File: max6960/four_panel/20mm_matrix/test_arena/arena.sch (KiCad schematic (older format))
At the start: 29 parts, among them P1 CONN15, P10 CONN_2X2, P11 CONN_2X2, P12 CONN_2X2, P13 CONN_2X2, P14 CONN_2X2, P15 CONN_2X2, P16 CONN_2X2, P17 CONN_2X2, P18 CONN_2X2, P19 CONN_2X2, P2 CONN15, P20 CONN_2X2, P21 CONN_2X2, P22 CONN_20X2, P23 CONN_30X2, P24 CONN_2, P3 CONN15, P4 CONN15, P5 CONN15, P6 CONN15, P7 CONN_2X2, P8 CONN_2X2, P9 CONN_2X2

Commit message: Finished 4x20mm matrix MAX6960 test arena.
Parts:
- added C6: 0.1uF, symbol C
- added P25: CONN_2X2, symbol CONN_2X2
- added P26: CONN_2, symbol CONN_2
- added U1: MAX7375, symbol MAX7375
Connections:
- net labels added: +3.3V, CLK_0, CLK_1, CLK_11, CLK_2, CLK_22, CLK_3, CLK_33, CLK_4, CLK_44, CLK_5, CLK_55, INT_OSC, OSC, OSC_EXT, OSC_INT, RST, VAUX
- net labels removed: +5V, EXT_INT0, EXT_INT1, RESET_MSTR, RX, SCK_0, SCK_1, SCK_11, SCK_2, SCK_22, SCK_3, SCK_33, SCK_4, SCK_44, SCK_5, SCK_55, TX
- wire segments 300 -> 299
- no-connect marks 3 -> 21
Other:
- note added: "Internal Oscillator"
- note added: "MAX7375AXR805+ (8MHz)"
- note added: "Oscillator Selection"
- moved on the sheet: C1, C2, C3, C4, C5, P22, P23, P24

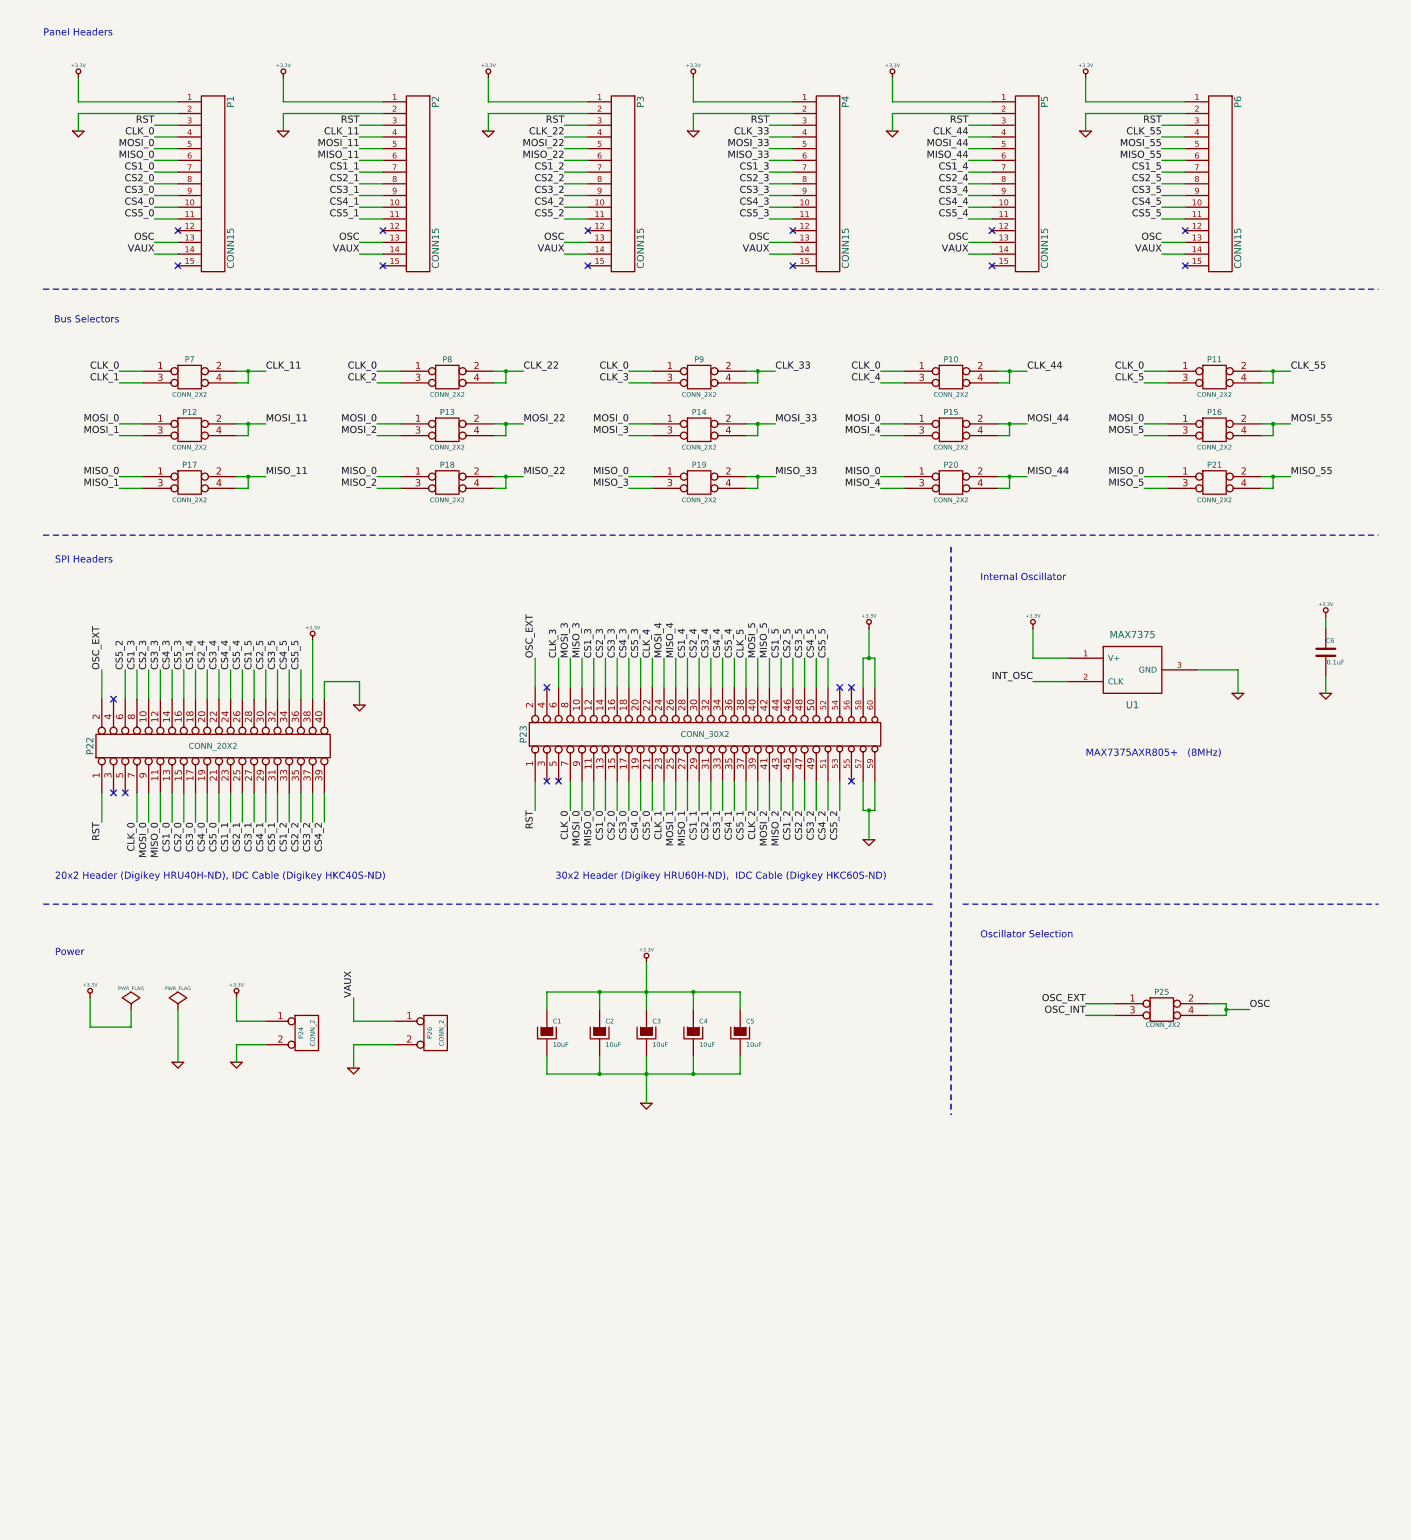
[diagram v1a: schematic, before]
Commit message: Added common CS SPI header to 4x20mm max6960 test arena. Fixed minor issue with 4x20mm atmega328 test arena.
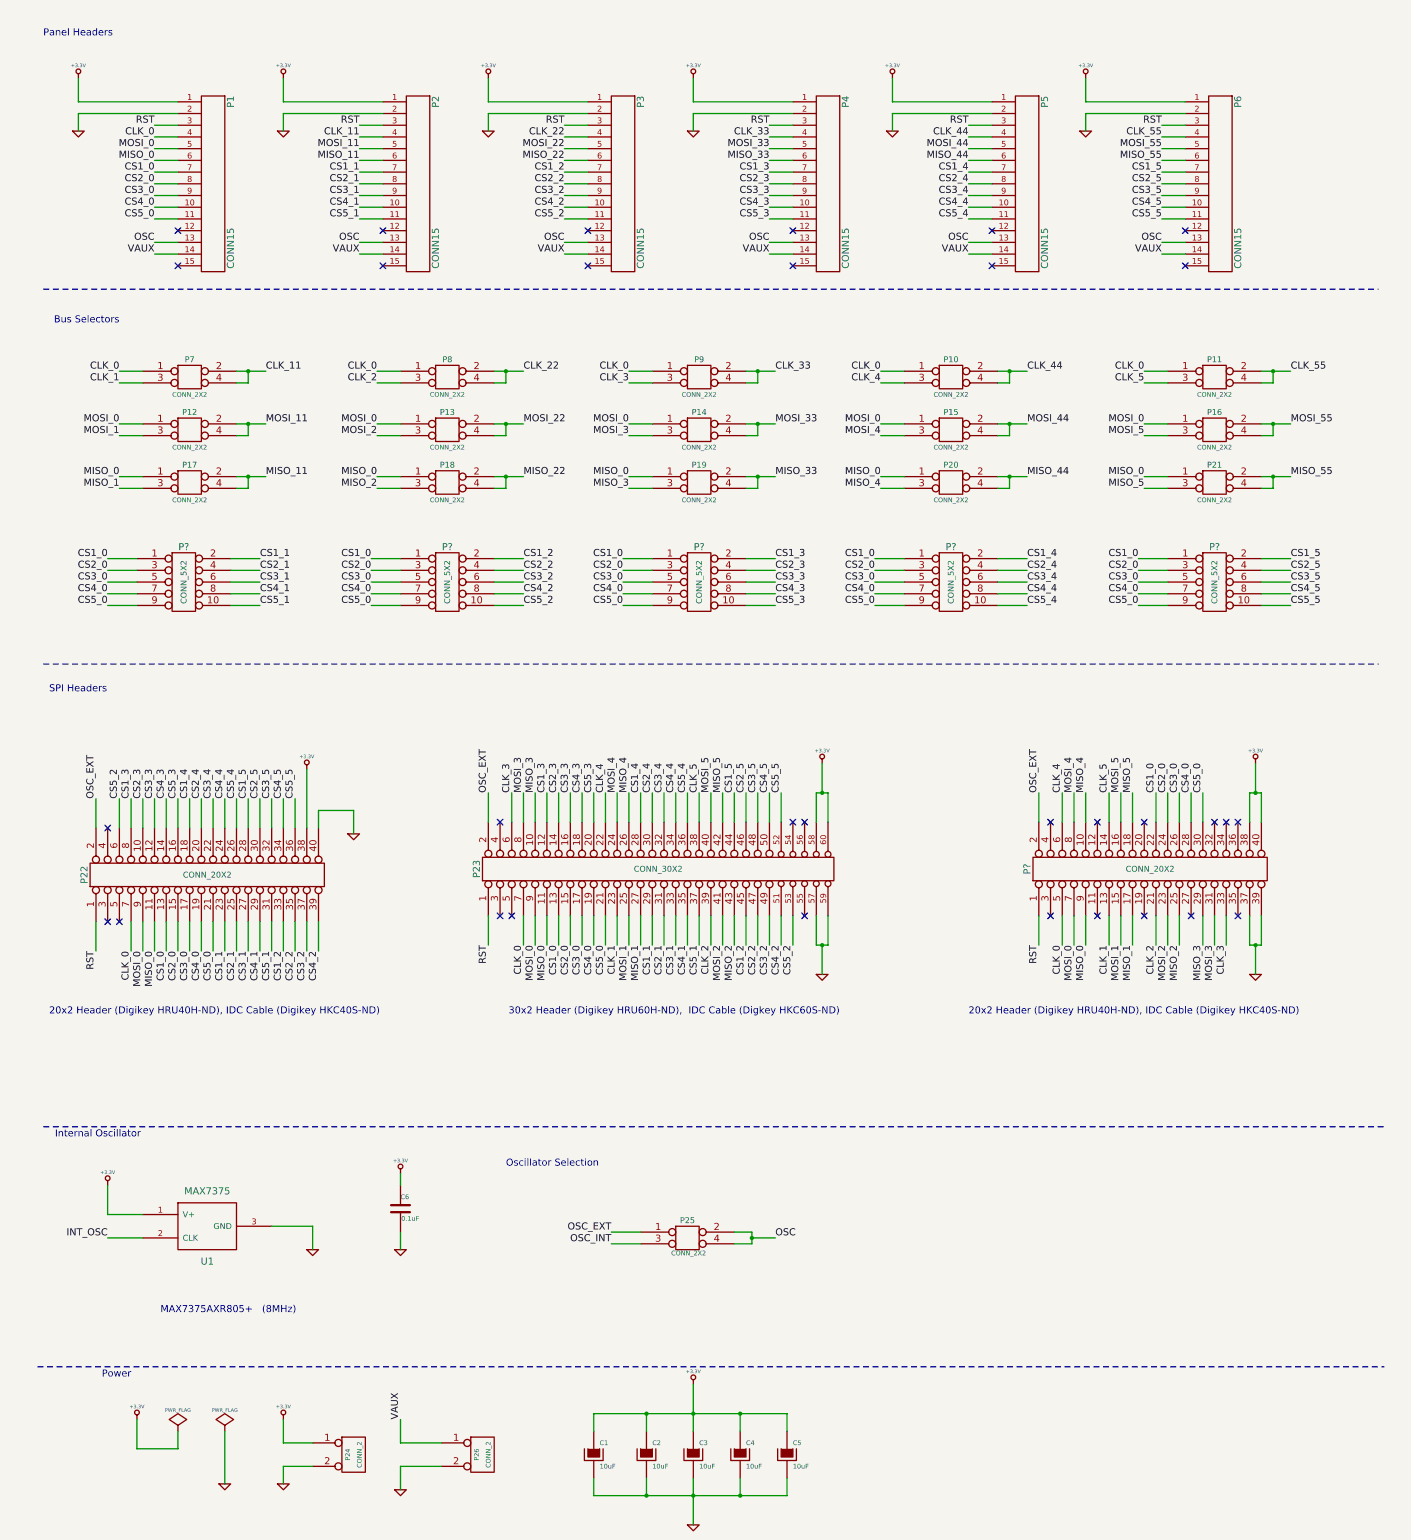
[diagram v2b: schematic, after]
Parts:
- added P? (x5): CONN_5X2, symbol CONN_5X2
- added P?: CONN_20X2, symbol CONN_20X2
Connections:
- net +3.3V: now also P?.38 (P38), P?.40 (P40)
- net CLK_0: now also P?.5 (P5)
- net CLK_1: now also P?.13 (P13)
- net CLK_2: now also P?.21 (P21)
- net CLK_3: now also P?.33 (P33)
- net CLK_4: now also P?.6 (P6)
- net CLK_5: now also P?.14 (P14)
- net CS1_0: now also P?.1, P?.1, P?.1, P?.1, P?.1, P?.22 (P22)
- net CS1_1: now also P?.2
- net CS1_2: now also P?.2
- net CS1_3: now also P?.2
- net CS1_4: now also P?.2
- net CS1_5: now also P?.2
- net CS2_0: now also P?.24 (P24), P?.3, P?.3, P?.3, P?.3, P?.3
- net CS2_1: now also P?.4
- net CS2_2: now also P?.4
- net CS2_3: now also P?.4
- net CS2_4: now also P?.4
- net CS2_5: now also P?.4
- net CS3_0: now also P?.26 (P26), P?.5, P?.5, P?.5, P?.5, P?.5
- net CS3_1: now also P?.6
- net CS3_2: now also P?.6
- net CS3_3: now also P?.6
- net CS3_4: now also P?.6
- net CS3_5: now also P?.6
- net CS4_0: now also P?.28 (P28), P?.7, P?.7, P?.7, P?.7, P?.7
- net CS4_1: now also P?.8
- net CS4_2: now also P?.8
- net CS4_3: now also P?.8
- net CS4_4: now also P?.8
- net CS4_5: now also P?.8
- net CS5_0: now also P?.30 (P30), P?.9, P?.9, P?.9, P?.9, P?.9
- net CS5_1: now also P?.10
- net CS5_2: now also P?.10
- net CS5_3: now also P?.10
- net CS5_4: now also P?.10
- net CS5_5: now also P?.10
- net GND: now also P?.37 (P37), P?.39 (P39)
- net MISO_0: now also P?.9 (P9)
- net MISO_1: now also P?.17 (P17)
- net MISO_2: now also P?.25
- net MISO_3: now also P?.29 (P29)
- net MISO_4: now also P?.10 (P10)
- net MISO_5: now also P?.18 (P18)
- net MOSI_0: now also P?.7 (P7)
- net MOSI_1: now also P?.15 (P15)
- net MOSI_2: now also P?.23 (P23)
- net MOSI_3: now also P?.31 (P31)
- net MOSI_4: now also P?.8 (P8)
- net MOSI_5: now also P?.16 (P16)
- net OSC_EXT: now also P?.2 (P2)
- net RST: now also P?.1 (P1)
- no-connect marks 21 -> 32
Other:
- moved on the sheet: C1, C2, C3, C4, C5, C6, P22, P23, P24, P25, P26, U1

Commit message: Added 3rd spi header to test arenas. Third header has 6 spi buses w/ 5 common cs lines.
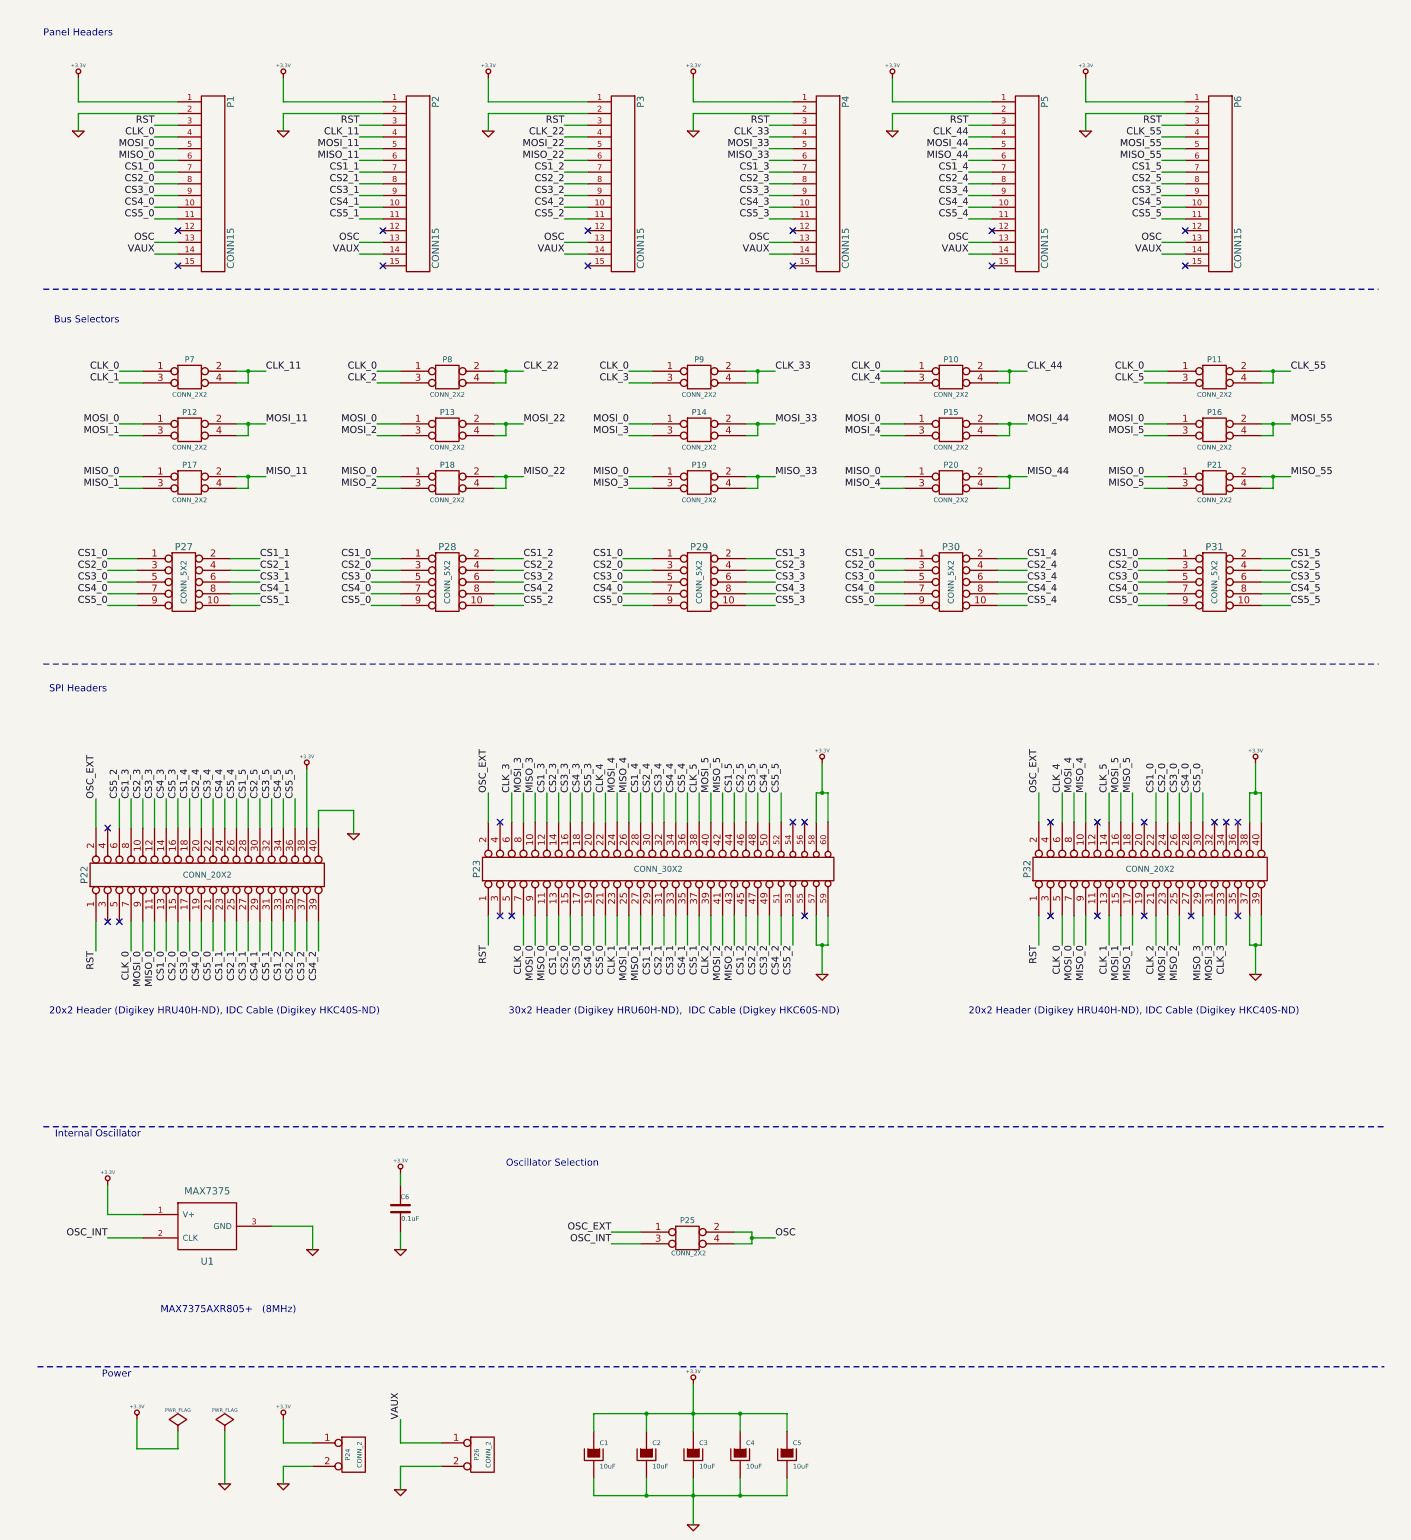
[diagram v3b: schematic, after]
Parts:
- gave numbers to parts that had none: 6
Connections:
- net INT_OSC is gone; now on net OSC_INT: U1.2 (CLK)
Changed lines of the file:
@@
 	1400 10900 1100 10900
 Text Label 1100 10900 2    60   ~ 0
-INT_OSC
+OSC_INT
 Text Notes 4500 10300 0    60   ~ 0
 Oscillator Selection
@@
 	500  12000 12000 12000
 $Comp
-L CONN_20X2 P?
+L CONN_20X2 P32
 U 1 1 52745EFE
 P 10000 7750
-F 0 "P?" H 10000 8800 60  0000 C CNN
+F 0 "P32" H 10000 8800 60  0000 C CNN
 F 1 "CONN_20X2" V 10000 7750 50  0000 C CNN
 F 2 "" H 10000 7750 60  0000 C CNN
@@
 Connection ~ 10900 8400
 $Comp
-L GND #PWR?
+L GND #PWR030
 U 1 1 52745F42
 P 10900 8650
-F 0 "#PWR?" H 10900 8650 30  0001 C CNN
+F 0 "#PWR030" H 10900 8650 30  0001 C CNN
 F 1 "GND" H 10900 8580 30  0001 C CNN
 F 2 "" H 10900 8650 60  0000 C CNN
@@
 OSC_EXT
 $Comp
-L +3.3V #PWR?
+L +3.3V #PWR031
 U 1 1 52745F7F
 P 10900 6850
-F 0 "#PWR?" H 10900 6810 30  0001 C CNN
+F 0 "#PWR031" H 10900 6810 30  0001 C CNN
 F 1 "+3.3V" H 10900 6960 30  0000 C CNN
 F 2 "" H 10900 6850 60  0000 C CNN
@@
 CS5_0
 $Comp
-L CONN_5X2 P?
+L CONN_5X2 P27
 U 1 1 52745D6C
 P 1750 5300
-F 0 "P?" H 1750 5600 60  0000 C CNN
+F 0 "P27" H 1750 5600 60  0000 C CNN
 F 1 "CONN_5X2" V 1750 5300 50  0000 C CNN
 F 2 "" H 1750 5300 60  0000 C CNN
@@
 $EndComp
 $Comp
-L CONN_5X2 P?
+L CONN_5X2 P28
 U 1 1 52745D7B
 P 4000 5300
-F 0 "P?" H 4000 5600 60  0000 C CNN
+F 0 "P28" H 4000 5600 60  0000 C CNN
 F 1 "CONN_5X2" V 4000 5300 50  0000 C CNN
 F 2 "" H 4000 5300 60  0000 C CNN
@@
 $EndComp
 $Comp
-L CONN_5X2 P?
+L CONN_5X2 P29
 U 1 1 52745D8A
 P 6150 5300
-F 0 "P?" H 6150 5600 60  0000 C CNN
+F 0 "P29" H 6150 5600 60  0000 C CNN
 F 1 "CONN_5X2" V 6150 5300 50  0000 C CNN
 F 2 "" H 6150 5300 60  0000 C CNN
@@
 $EndComp
 $Comp
-L CONN_5X2 P?
+L CONN_5X2 P30
 U 1 1 52745D99
 P 8300 5300
-F 0 "P?" H 8300 5600 60  0000 C CNN
+F 0 "P30" H 8300 5600 60  0000 C CNN
 F 1 "CONN_5X2" V 8300 5300 50  0000 C CNN
 F 2 "" H 8300 5300 60  0000 C CNN
@@
 $EndComp
 $Comp
-L CONN_5X2 P?
+L CONN_5X2 P31
 U 1 1 52745DA8
 P 10550 5300
-F 0 "P?" H 10550 5600 60  0000 C CNN
+F 0 "P31" H 10550 5600 60  0000 C CNN
 F 1 "CONN_5X2" V 10550 5300 50  0000 C CNN
 F 2 "" H 10550 5300 60  0000 C CNN
